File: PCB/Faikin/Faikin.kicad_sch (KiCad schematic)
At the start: 27 parts, among them J1 1x5, J2 Conn_01x06, Q1 BSS138PS, U2 ESP32-S3-MINI-1, U3 MD8942

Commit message: TC2030-USB-NL cable pin out
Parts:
- removed J2: Conn_01x06, RevK:Tag-Connect_TC2030-IDC-NL_2x03_P1.27mm_Vertical, symbol Connector_Generic:Conn_01x06
- added J3: TC2030-USB-NL, RevK:Tag-Connect_TC2030-IDC-NL_2x03_P1.27mm_Vertical, symbol Connector_Generic:Conn_01x06
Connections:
- net D+: now also J3.4 (Pin_4)
- net D-: now also J3.3 (Pin_3)
- net DC: now also J3.1 (Pin_1), J3.2 (Pin_2)
- net GND: now also J3.5 (Pin_5), J3.6 (Pin_6)

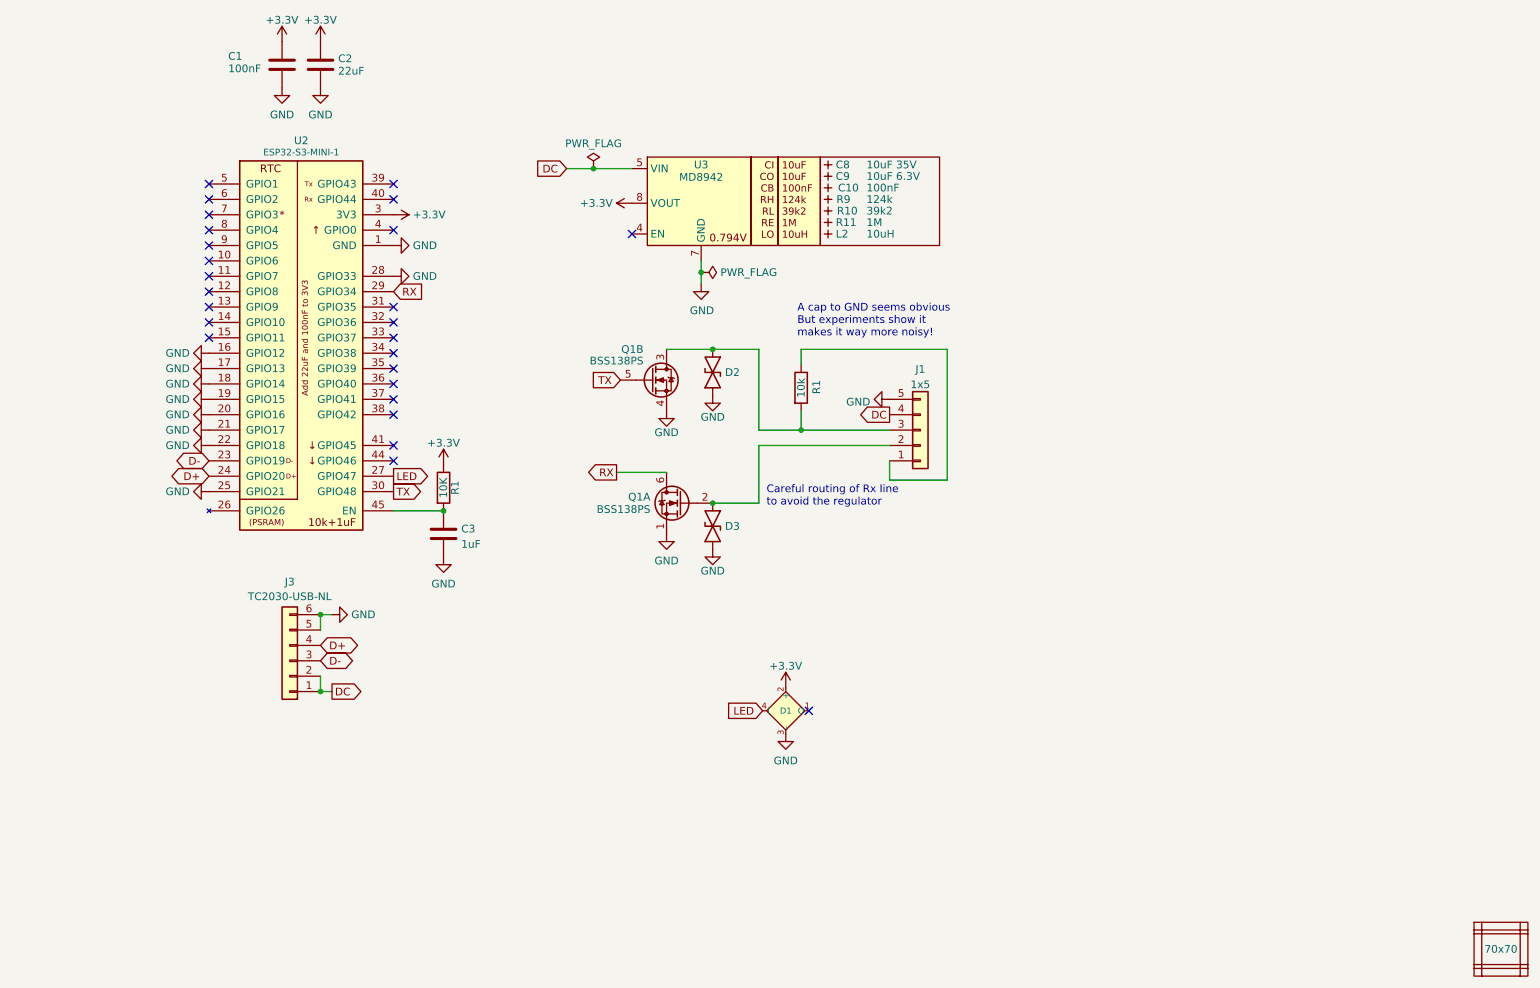
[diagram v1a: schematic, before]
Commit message: Reworked for TC2030-USB-NL
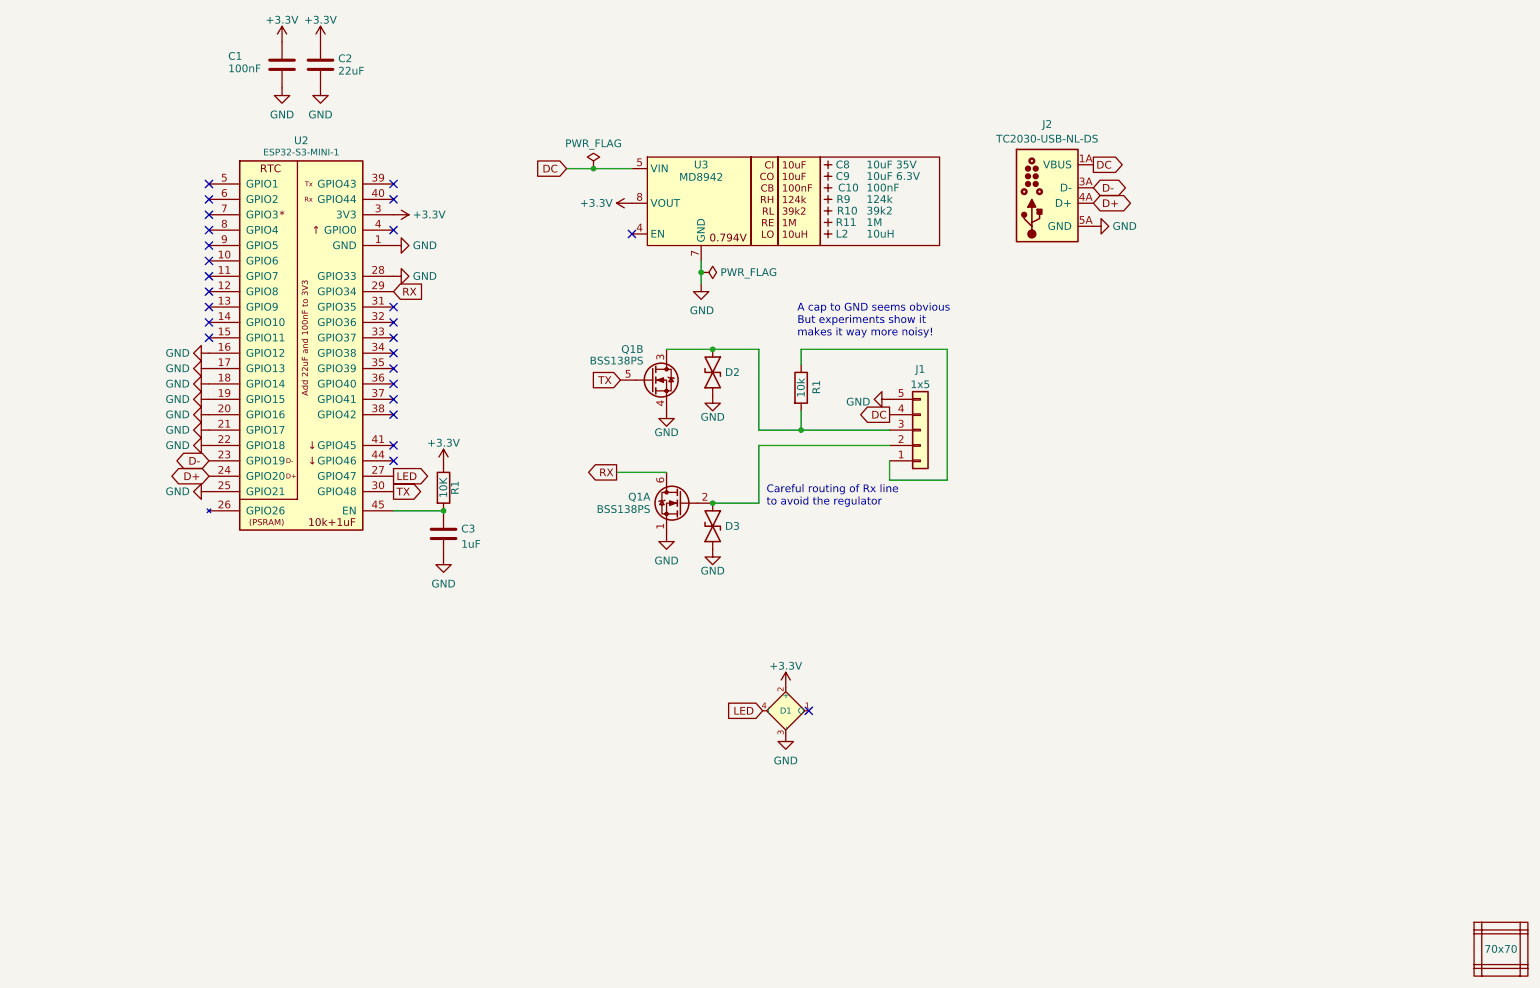
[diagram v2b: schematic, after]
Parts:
- removed J3: TC2030-USB-NL, RevK:Tag-Connect_TC2030-IDC-NL_2x03_P1.27mm_Vertical, symbol Connector_Generic:Conn_01x06
- added J2: TC2030-USB-NL-DS, RevK:Tag-Connect_TC2030-IDC-NL_2x03_P1.27mm_Vertical_DoubleSided, symbol RevK:TC2030-USB-NL-DS
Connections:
- net D+: now also J2.4A (D+), J2.4B (D+)
- net D-: now also J2.3A (D-), J2.3B (D-)
- net DC: now also J2.1A (VBUS), J2.1B (VBUS), J2.2A (VBUS), J2.2B (VBUS)
- net GND: now also J2.5A (GND), J2.5B (GND), J2.6A (GND), J2.6B (GND)

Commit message: Tweaked PCb
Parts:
- J2: footprint RevK:Tag-Connect_TC2030-IDC-NL_2x03_P1.27mm_Vertical_DoubleSided -> RevK:Tag-Connect_TC2030-IDC-NL_2x03_P1.27mm_Vertical; symbol RevK:TC2030-USB-NL-DS -> RevK:TC2030-USB-NL
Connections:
- net +3.3V: now also U2.19 (GPIO15)
- net D+: now also J2.4 (D+); no longer J2.4A (D+), J2.4B (D+)
- net D-: now also J2.3 (D-); no longer J2.3A (D-), J2.3B (D-)
- net DC: now also J2.1 (VBUS), J2.2 (VBUS); no longer J2.1A (VBUS), J2.1B (VBUS), J2.2A (VBUS), J2.2B (VBUS)
- net GND: now also J2.5 (GND), J2.6 (GND); no longer J2.5A (GND), J2.5B (GND), J2.6A (GND), J2.6B (GND), U2.19 (GPIO15)
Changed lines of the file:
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@@
 	)
 	(symbol
-		(lib_id "RevK:TC2030-USB-NL-DS")
+		(lib_id "RevK:TC2030-USB-NL")
 		(at 187.325 49.53 0)
 		(unit 1)
@@
 			)
 		)
-		(property "Footprint" "RevK:Tag-Connect_TC2030-IDC-NL_2x03_P1.27mm_Vertical_DoubleSided"
+		(property "Footprint" "RevK:Tag-Connect_TC2030-IDC-NL_2x03_P1.27mm_Vertical"
 			(at 187.071 58.674 0)
 			(effects
@@
 			)
 		)
-		(property "Description" "TC2030-USB-NL-DS"
+		(property "Description" "TC2030-USB-NL"
 			(at 187.325 36.83 0)
 			(effects
@@
 			)
 		)
-		(pin "1A"
-		)
-		(pin "1B"
-		)
-		(pin "2A"
-		)
-		(pin "2B"
-		)
-		(pin "3A"
-		)
-		(pin "3B"
-		)
-		(pin "4A"
-		)
-		(pin "4B"
-		)
-		(pin "5A"
-		)
-		(pin "5B"
-		)
-		(pin "6A"
-		)
-		(pin "6B"
+		(pin "5"
+		)
+		(pin "6"
+		)
+		(pin "1"
+		)
+		(pin "4"
+		)
+		(pin "3"
+		)
+		(pin "2"
 		)
 		(instances
@@
 	)
 	(symbol
-		(lib_id "power:GND")
-		(at 48.895 83.185 270)
-		(unit 1)
-		(exclude_from_sim no)
-		(in_bom yes)
-		(on_board yes)
-		(dnp no)
-		(fields_autoplaced yes)
-		(property "Reference" "#PWR01"
-			(at 42.545 83.185 0)
-			(effects
-				(font
-					(size 1.27 1.27)
-				)
-				(hide yes)
-			)
-		)
-		(property "Value" "GND"
-			(at 45.7201 83.185 90)
-			(effects
-				(font
-					(size 1.27 1.27)
-				)
-				(justify right)
-			)
-		)
-		(property "Footprint" ""
-			(at 48.895 83.185 0)
-			(effects
-				(font
-					(size 1.27 1.27)
-				)
-				(hide yes)
-			)
-		)
-		(property "Datasheet" ""
-			(at 48.895 83.185 0)
-			(effects
-				(font
-					(size 1.27 1.27)
-				)
-				(hide yes)
-			)
-		)
-		(property "Description" "Power symbol creates a global label with name \"GND\" , ground"
-			(at 48.895 83.185 0)
-			(effects
-				(font
-					(size 1.27 1.27)
-				)
-				(hide yes)
-			)
-		)
-		(pin "1"
-		)
-		(instances
-			(project "USBA"
-				(path "/2d210a96-f81f-42a9-8bf4-1b43c11086f3"
-					(reference "#PWR01")
-					(unit 1)
-				)
-			)
-			(project "Faikin"
-				(path "/46c350bb-7de4-4e81-aafd-4af55e37aab0"
-					(reference "#PWR020")
-					(unit 1)
-				)
-			)
-		)
-	)
-	(symbol
 		(lib_id "RevK:Hidden")
 		(at 151.13 55.88 90)
@@
 					(unit 1)
 				)
+			)
+		)
+	)
+	(symbol
+		(lib_id "power:+3.3V")
+		(at 48.895 83.185 90)
+		(unit 1)
+		(exclude_from_sim no)
+		(in_bom yes)
+		(on_board yes)
+		(dnp no)
+		(fields_autoplaced yes)
+		(property "Reference" "#PWR020"
+			(at 52.705 83.185 0)
+			(effects
+				(font
+					(size 1.27 1.27)
+				)
+				(hide yes)
+			)
+		)
+		(property "Value" "+3.3V"
+			(at 45.72 83.185 90)
+			(effects
+				(font
+					(size 1.27 1.27)
+				)
+				(justify left)
+			)
+		)
+		(property "Footprint" ""
+			(at 48.895 83.185 0)
+			(effects
+				(font
+					(size 1.27 1.27)
+				)
+				(hide yes)
+			)
+		)
+		(property "Datasheet" ""
+			(at 48.895 83.185 0)
+			(effects
+				(font
+					(size 1.27 1.27)
+				)
+				(hide yes)
+			)
+		)
+		(property "Description" "Power symbol creates a global label with name \"+3.3V\""
+			(at 48.895 83.185 0)
+			(effects
+				(font
+					(size 1.27 1.27)
+				)
+				(hide yes)
+			)
+		)
+		(pin "1"
+		)
+		(instances
+			(project "Faikin"
+				(path "/46c350bb-7de4-4e81-aafd-4af55e37aab0"
+					(reference "#PWR020")
+					(unit 1)
+				)

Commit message: Tidy PCb
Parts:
- added TP1, TP2: TestPoint, TestPoint:TestPoint_Pad_2.0x2.0mm, symbol Connector:TestPoint
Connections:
- net GND: now also TP2.1; no longer U2.25 (GPIO21)
- new net: TP1.1, U2.25 (GPIO21)
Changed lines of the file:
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@@
 	(wire
 		(pts
+			(xy 29.845 98.425) (xy 48.895 98.425)
+		)
+		(stroke
+			(width 0)
+			(type default)
+		)
+	)
+	(wire
+		(pts
 			(xy 124.46 74.93) (xy 132.08 74.93)
 		)
@@
 	)
 	(symbol
+		(lib_id "Connector:TestPoint")
+		(at 26.67 98.425 0)
+		(unit 1)
+		(exclude_from_sim no)
+		(in_bom yes)
+		(on_board yes)
+		(dnp no)
+		(property "Reference" "TP2"
+			(at 21.463 93.472 0)
+			(effects
+				(font
+					(size 1.27 1.27)
+				)
+				(justify left)
+			)
+		)
+		(property "Value" "TestPoint"
+			(at 16.383 96.266 0)
+			(effects
+				(font
+					(size 1.27 1.27)
+				)
+				(justify left)
+			)
+		)
+		(property "Footprint" "TestPoint:TestPoint_Pad_2.0x2.0mm"
+			(at 31.75 98.425 0)
+			(effects
+				(font
+					(size 1.27 1.27)
+				)
+				(hide yes)
+			)
+		)
+		(property "Datasheet" "~"
+			(at 31.75 98.425 0)
+			(effects
+				(font
+					(size 1.27 1.27)
+				)
+				(hide yes)
+			)
+		)
+		(property "Description" "test point"
+			(at 26.67 98.425 0)
+			(effects
+				(font
+					(size 1.27 1.27)
+				)
+				(hide yes)
+			)
+		)
+		(pin "1"
+		)
+		(instances
+			(project "Faikin"
+				(path "/46c350bb-7de4-4e81-aafd-4af55e37aab0"
+					(reference "TP2")
+					(unit 1)
+				)
+			)
+		)
+	)
+	(symbol
 		(lib_id "RevK:VCUT")
 		(at 259.08 173.99 90)
@@
 	(symbol
 		(lib_id "power:GND")
-		(at 48.895 98.425 270)
+		(at 48.895 90.805 270)
 		(unit 1)
 		(exclude_from_sim no)
@@
 		(fields_autoplaced yes)
 		(property "Reference" "#PWR026"
-			(at 42.545 98.425 0)
+			(at 42.545 90.805 0)
 			(effects
 				(font
@@
 		)
 		(property "Value" "GND"
-			(at 45.7201 98.425 90)
+			(at 45.7201 90.805 90)
 			(effects
 				(font
@@
 		)
 		(property "Footprint" ""
-			(at 48.895 98.425 0)
+			(at 48.895 90.805 0)
 			(effects
 				(font
@@
 		)
 		(property "Datasheet" ""
-			(at 48.895 98.425 0)
+			(at 48.895 90.805 0)
 			(effects
 				(font
@@
 		)
 		(property "Description" "Power symbol creates a global label with name \"GND\" , ground"
-			(at 48.895 98.425 0)
+			(at 48.895 90.805 0)
 			(effects
 				(font
@@
 	(symbol
 		(lib_id "power:GND")
-		(at 48.895 90.805 270)
+		(at 26.67 98.425 0)
 		(unit 1)
 		(exclude_from_sim no)
@@
 		(dnp no)
 		(fields_autoplaced yes)
-		(property "Reference" "#PWR01"
-			(at 42.545 90.805 0)
+		(property "Reference" "#PWR017"
+			(at 26.67 104.775 0)
 			(effects
 				(font
@@
 		)
 		(property "Value" "GND"
-			(at 45.7201 90.805 90)
+			(at 26.67 102.5581 0)
 			(effects
 				(font
 					(size 1.27 1.27)
 				)
-				(justify right)
 			)
 		)
 		(property "Footprint" ""
-			(at 48.895 90.805 0)
+			(at 26.67 98.425 0)
 			(effects
 				(font
@@
 		)
 		(property "Datasheet" ""
-			(at 48.895 90.805 0)
+			(at 26.67 98.425 0)
 			(effects
 				(font
@@
 		)
 		(property "Description" "Power symbol creates a global label with name \"GND\" , ground"
-			(at 48.895 90.805 0)
+			(at 26.67 98.425 0)
 			(effects
 				(font
@@
 		)
 		(instances
-			(project "USBA"
-				(path "/2d210a96-f81f-42a9-8bf4-1b43c11086f3"
-					(reference "#PWR01")
-					(unit 1)
-				)
-			)
 			(project "Faikin"
 				(path "/46c350bb-7de4-4e81-aafd-4af55e37aab0"
@@
 					(unit 1)
 				)
+			)
+		)
+	)
+	(symbol
+		(lib_id "Connector:TestPoint")
+		(at 29.845 98.425 0)
+		(unit 1)
+		(exclude_from_sim no)
+		(in_bom yes)
+		(on_board yes)
+		(dnp no)
+		(fields_autoplaced yes)
+		(property "Reference" "TP1"
+			(at 31.242 93.9108 0)
+			(effects
+				(font
+					(size 1.27 1.27)
+				)
+				(justify left)
+			)
+		)
+		(property "Value" "TestPoint"
+			(at 31.242 96.3351 0)
+			(effects
+				(font
+					(size 1.27 1.27)
+				)
+				(justify left)
+			)
+		)
+		(property "Footprint" "TestPoint:TestPoint_Pad_2.0x2.0mm"
+			(at 34.925 98.425 0)
+			(effects
+				(font
+					(size 1.27 1.27)
+				)
+				(hide yes)
+			)
+		)
+		(property "Datasheet" "~"
+			(at 34.925 98.425 0)
+			(effects
+				(font
+					(size 1.27 1.27)
+				)
+				(hide yes)
+			)
+		)
+		(property "Description" "test point"
+			(at 29.845 98.425 0)
+			(effects
+				(font
+					(size 1.27 1.27)
+				)
+				(hide yes)
+			)
+		)
+		(pin "1"
+		)
+		(instances
+			(project ""
+				(path "/46c350bb-7de4-4e81-aafd-4af55e37aab0"
+					(reference "TP1")
+					(unit 1)
+				)

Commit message: TPs
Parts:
- TP1, TP2: now left out of the parts list
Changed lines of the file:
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@@
 		(unit 1)
 		(exclude_from_sim no)
-		(in_bom yes)
+		(in_bom no)
 		(on_board yes)
 		(dnp no)
@@
 		(unit 1)
 		(exclude_from_sim no)
-		(in_bom yes)
-		(on_board yes)
-		(dnp no)
+		(in_bom no)
+		(on_board yes)
+		(dnp no)

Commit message: Style
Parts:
- removed TP1, TP2: TestPoint, TestPoint:TestPoint_Pad_2.0x2.0mm, symbol Connector:TestPoint
- added J3: Reset, RevK:AA-Pad, symbol Connector_Generic:Conn_01x02
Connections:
- net GND: now also J3.1 (Pin_1)
- net at U2.25 (GPIO21): now also J3.2 (Pin_2)
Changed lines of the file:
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@@
 	(wire
 		(pts
-			(xy 29.845 98.425) (xy 48.895 98.425)
+			(xy 36.83 98.425) (xy 48.895 98.425)
 		)
 		(stroke
@@
 	)
 	(symbol
-		(lib_id "Connector:TestPoint")
-		(at 26.67 98.425 0)
-		(unit 1)
-		(exclude_from_sim no)
-		(in_bom no)
-		(on_board yes)
-		(dnp no)
-		(property "Reference" "TP2"
-			(at 21.463 93.472 0)
-			(effects
-				(font
-					(size 1.27 1.27)
-				)
-				(justify left)
-			)
-		)
-		(property "Value" "TestPoint"
-			(at 16.383 96.266 0)
-			(effects
-				(font
-					(size 1.27 1.27)
-				)
-				(justify left)
-			)
-		)
-		(property "Footprint" "TestPoint:TestPoint_Pad_2.0x2.0mm"
-			(at 31.75 98.425 0)
-			(effects
-				(font
-					(size 1.27 1.27)
-				)
-				(hide yes)
-			)
-		)
-		(property "Datasheet" "~"
-			(at 31.75 98.425 0)
-			(effects
-				(font
-					(size 1.27 1.27)
-				)
-				(hide yes)
-			)
-		)
-		(property "Description" "test point"
-			(at 26.67 98.425 0)
-			(effects
-				(font
-					(size 1.27 1.27)
-				)
-				(hide yes)
-			)
-		)
-		(pin "1"
-		)
-		(instances
-			(project "Faikin"
-				(path "/46c350bb-7de4-4e81-aafd-4af55e37aab0"
-					(reference "TP2")
-					(unit 1)
-				)
-			)
-		)
-	)
-	(symbol
 		(lib_id "RevK:VCUT")
 		(at 259.08 173.99 90)
@@
 	)
 	(symbol
+		(lib_id "Connector_Generic:Conn_01x02")
+		(at 31.75 100.965 180)
+		(unit 1)
+		(exclude_from_sim no)
+		(in_bom yes)
+		(on_board yes)
+		(dnp no)
+		(fields_autoplaced yes)
+		(property "Reference" "J3"
+			(at 31.75 93.0105 0)
+			(effects
+				(font
+					(size 1.27 1.27)
+				)
+			)
+		)
+		(property "Value" "Reset"
+			(at 31.75 95.4348 0)
+			(effects
+				(font
+					(size 1.27 1.27)
+				)
+			)
+		)
+		(property "Footprint" "RevK:AA-Pad"
+			(at 31.75 100.965 0)
+			(effects
+				(font
+					(size 1.27 1.27)
+				)
+				(hide yes)
+			)
+		)
+		(property "Datasheet" "~"
+			(at 31.75 100.965 0)
+			(effects
+				(font
+					(size 1.27 1.27)
+				)
+				(hide yes)
+			)
+		)
+		(property "Description" "Generic connector, single row, 01x02, script generated (kicad-library-utils/schlib/autogen/connector/)"
+			(at 31.75 100.965 0)
+			(effects
+				(font
+					(size 1.27 1.27)
+				)
+				(hide yes)
+			)
+		)
+		(pin "2"
+		)
+		(pin "1"
+		)
+		(instances
+			(project ""
+				(path "/46c350bb-7de4-4e81-aafd-4af55e37aab0"
+					(reference "J3")
+					(unit 1)
+				)
+			)
+		)
+	)
+	(symbol
 		(lib_id "power:GND")
 		(at 130.175 64.135 0)
@@
 	(symbol
 		(lib_id "power:GND")
-		(at 26.67 98.425 0)
+		(at 36.83 100.965 90)
 		(unit 1)
 		(exclude_from_sim no)
@@
 		(fields_autoplaced yes)
 		(property "Reference" "#PWR017"
-			(at 26.67 104.775 0)
+			(at 43.18 100.965 0)
 			(effects
 				(font
@@
 		)
 		(property "Value" "GND"
-			(at 26.67 102.5581 0)
+			(at 40.005 100.965 90)
 			(effects
 				(font
 					(size 1.27 1.27)
 				)
+				(justify right)
 			)
 		)
 		(property "Footprint" ""
-			(at 26.67 98.425 0)
+			(at 36.83 100.965 0)
 			(effects
 				(font
@@
 		)
 		(property "Datasheet" ""
-			(at 26.67 98.425 0)
+			(at 36.83 100.965 0)
 			(effects
 				(font
@@
 		)
 		(property "Description" "Power symbol creates a global label with name \"GND\" , ground"
-			(at 26.67 98.425 0)
+			(at 36.83 100.965 0)
 			(effects
 				(font
@@
 					(unit 1)
 				)
-			)
-		)
-	)
-	(symbol
-		(lib_id "Connector:TestPoint")
-		(at 29.845 98.425 0)
-		(unit 1)
-		(exclude_from_sim no)
-		(in_bom no)
-		(on_board yes)
-		(dnp no)
-		(fields_autoplaced yes)
-		(property "Reference" "TP1"
-			(at 31.242 93.9108 0)
-			(effects
-				(font
-					(size 1.27 1.27)
-				)
-				(justify left)
-			)
-		)
-		(property "Value" "TestPoint"
-			(at 31.242 96.3351 0)
-			(effects
-				(font
-					(size 1.27 1.27)
-				)
-				(justify left)
-			)
-		)
-		(property "Footprint" "TestPoint:TestPoint_Pad_2.0x2.0mm"
-			(at 34.925 98.425 0)
-			(effects
-				(font
-					(size 1.27 1.27)
-				)
-				(hide yes)
-			)
-		)
-		(property "Datasheet" "~"
-			(at 34.925 98.425 0)
-			(effects
-				(font
-					(size 1.27 1.27)
-				)
-				(hide yes)
-			)
-		)
-		(property "Description" "test point"
-			(at 29.845 98.425 0)
-			(effects
-				(font
-					(size 1.27 1.27)
-				)
-				(hide yes)
-			)
-		)
-		(pin "1"
-		)
-		(instances
-			(project ""
-				(path "/46c350bb-7de4-4e81-aafd-4af55e37aab0"
-					(reference "TP1")
-					(unit 1)
-				)

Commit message: PCb tweaks
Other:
- moved on the sheet: C1, C10, C2, C3, C8, C9, D1, D2, D3, J1, J2, J3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
